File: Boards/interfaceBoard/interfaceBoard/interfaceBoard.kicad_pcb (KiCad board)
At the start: 2 copper layers, 100 x 100 mm, 24 parts, among them J1 Interface With Arduino, U1 74HC595, U2 TBD62783A, U3 74HC165

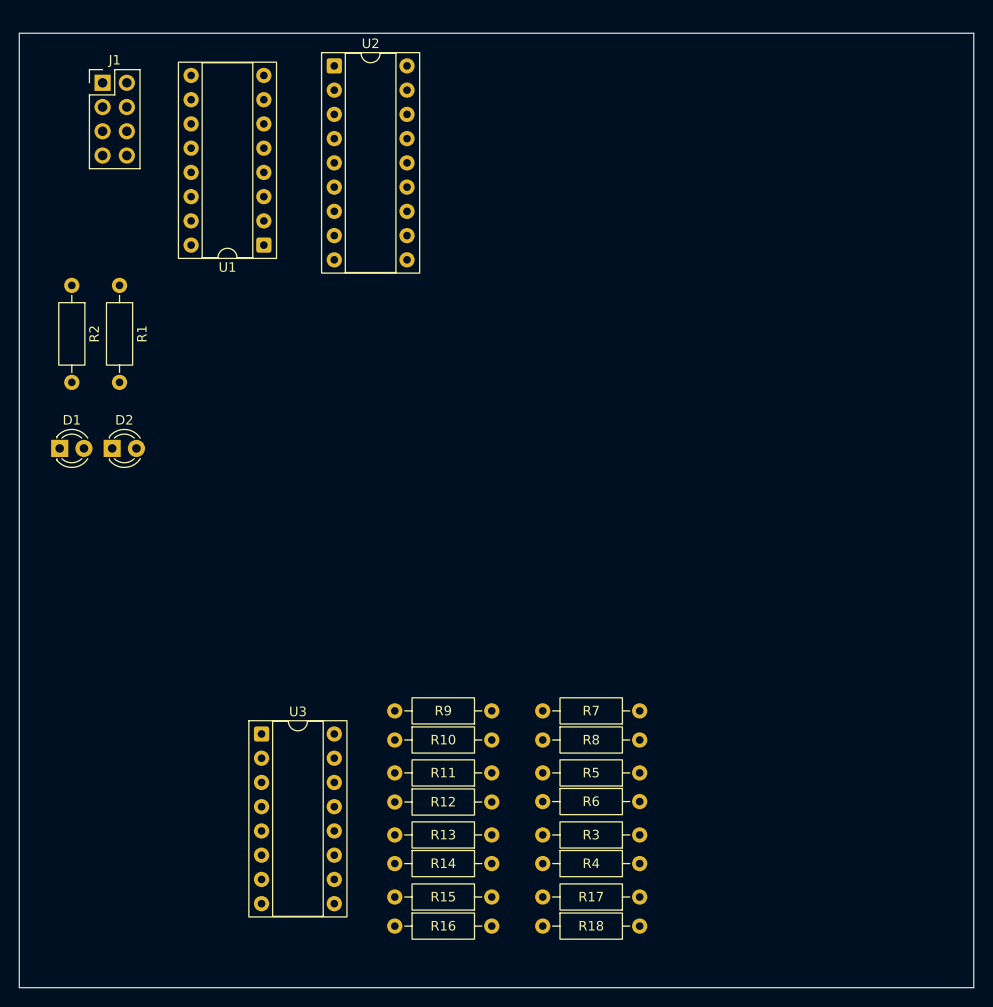
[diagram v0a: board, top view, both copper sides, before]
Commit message: Reapply "Auto pull push"
This reverts commit db7917ef1da9a17ad60c6a8d24e2f094312c5eaa.
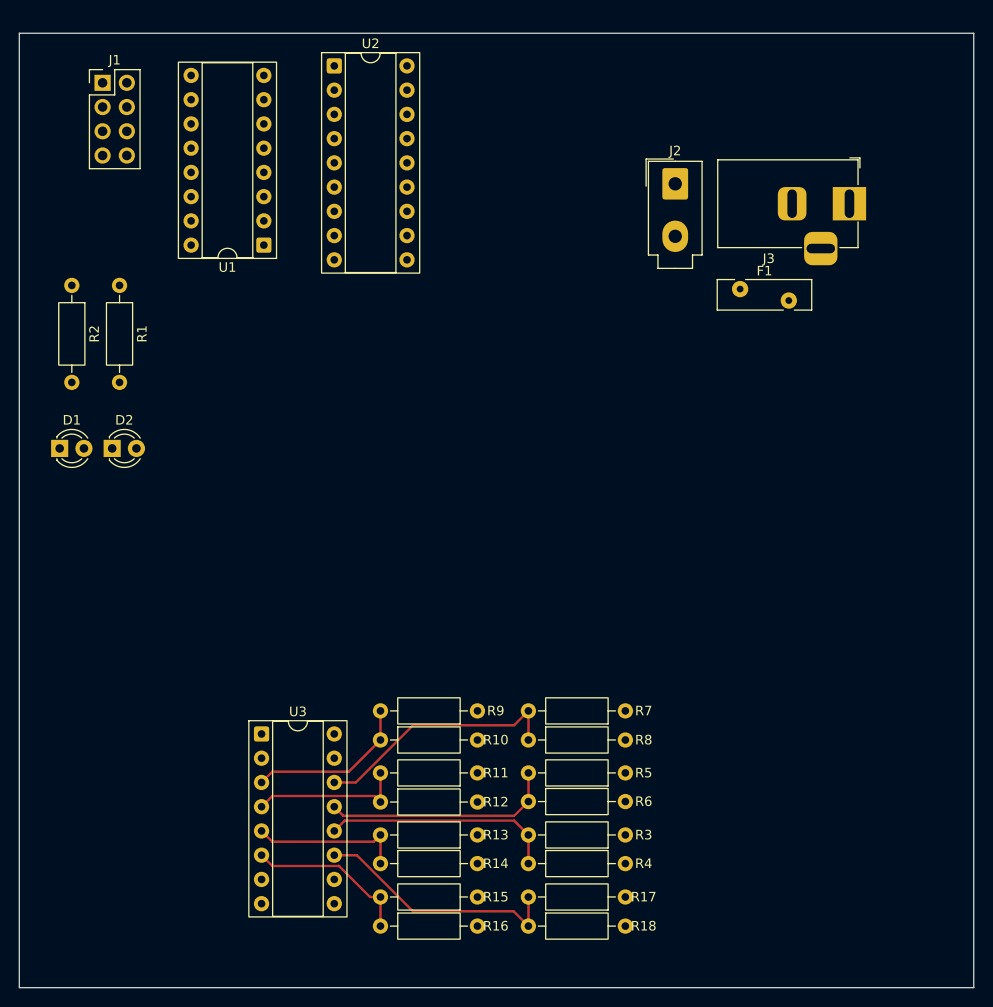
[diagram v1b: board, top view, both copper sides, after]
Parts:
- added F1: Polyfuse, Fuse:Fuse_Bourns_MF-RHT100, F.Cu at (125.5, 76.8)
- added J2: 12V input (molex), Connector_Molex:Molex_Mini-Fit_Jr_5566-02A_2x01_P4.20mm_Vertical, F.Cu at (118.7, 65.8)
- added J3: Barrel_Jack_Switch, Connector_BarrelJack:BarrelJack_Horizontal, F.Cu at (137.0, 67.9)
- moved R10 1.50 mm to (87.8, 124.0)
- moved R11 1.50 mm to (98.0, 127.5)
- moved R12 1.50 mm to (87.8, 130.6)
- moved R13 1.50 mm to (98.0, 134.0)
- moved R14 1.50 mm to (87.8, 137.0)
- moved R15 1.50 mm to (98.0, 140.5)
- moved R16 1.50 mm to (87.8, 143.6)
- moved R17 1.50 mm to (113.5, 140.5)
- moved R18 1.50 mm to (103.3, 143.6)
- moved R3 1.50 mm to (113.5, 134.0)
- moved R4 1.50 mm to (103.3, 137.0)
- moved R5 1.50 mm to (113.5, 127.5)
- moved R6 1.50 mm to (103.3, 130.5)
- moved R7 1.50 mm to (113.5, 121.0)
- moved R8 1.50 mm to (103.3, 124.0)
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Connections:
- net /MISO_sheet/D0 renamed /D0
- net /MISO_sheet/D1 renamed /D1
- net /MISO_sheet/D2 renamed /D2
- net /MISO_sheet/D3 renamed /D3
- net /MISO_sheet/D4 renamed /D4
- net /MISO_sheet/D5 renamed /D5
- net /MISO_sheet/D6 renamed /D6
- net /MISO_sheet/D7 renamed /D7
- net /MISO_sheet/SerIn renamed /SIN0
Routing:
- net /MISO_sheet/vDiv3/OUT: track 0.00 -> 26.5 mm
- net /MISO_sheet/vDiv0/OUT: track 0.00 -> 26.5 mm
- net /MISO_sheet/vDiv1/OUT: track 0.00 -> 24.4 mm
- net /MISO_sheet/vDiv2/OUT: track 0.00 -> 24.4 mm
- net /MISO_sheet/vDiv4/OUT: track 0.00 -> 17.4 mm
- net /MISO_sheet/vDiv7/OUT: track 0.00 -> 17.3 mm
- net /MISO_sheet/vDiv5/OUT: track 0.00 -> 16.2 mm
- net /MISO_sheet/vDiv6/OUT: track 0.00 -> 16.2 mm

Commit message: interface board work
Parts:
- moved J3 72.5 mm to (64.5, 70.5)
- moved J2 64.6 mm to (56.5, 83.2)
- moved D1 54.3 mm to (106.7, 107.5)
- moved D2 54.3 mm to (112.2, 107.5)
- moved R1 54.3 mm to (113.0, 90.4)
- moved R2 54.3 mm to (108.0, 90.4)
- moved F1 54.3 mm to (71.5, 81.4)
- moved U1 18.6 mm to (94.1, 70.7)
- moved U2 18.6 mm to (101.5, 51.9)
- moved J1 4.47 mm to (54.7, 53.2)
